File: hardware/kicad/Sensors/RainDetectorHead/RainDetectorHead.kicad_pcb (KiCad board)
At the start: 2 copper layers, 54.1 x 44.1 mm, 27 parts, among them J1 Conn_01x04_Pin, J2 Conn_01x04_Pin

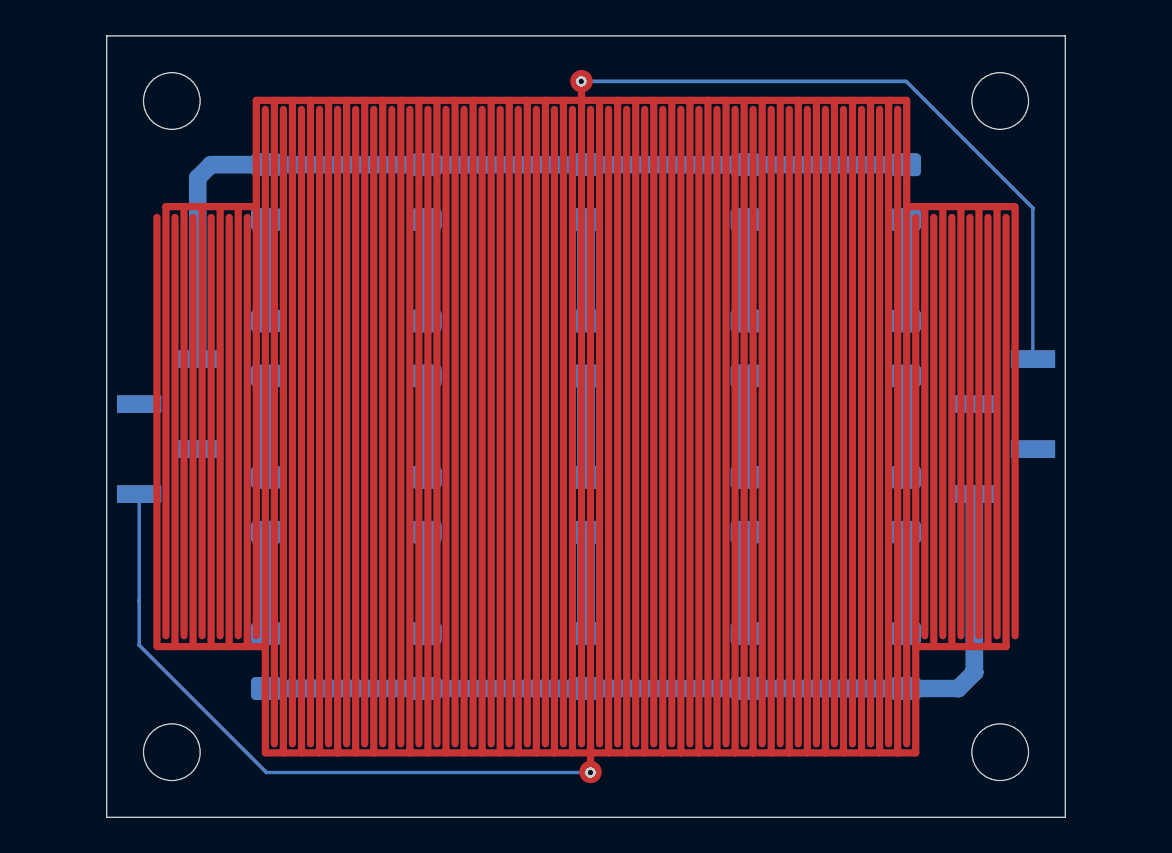
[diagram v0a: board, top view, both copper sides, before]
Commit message: modified Board-Geometry for RainDetector Head & Controller
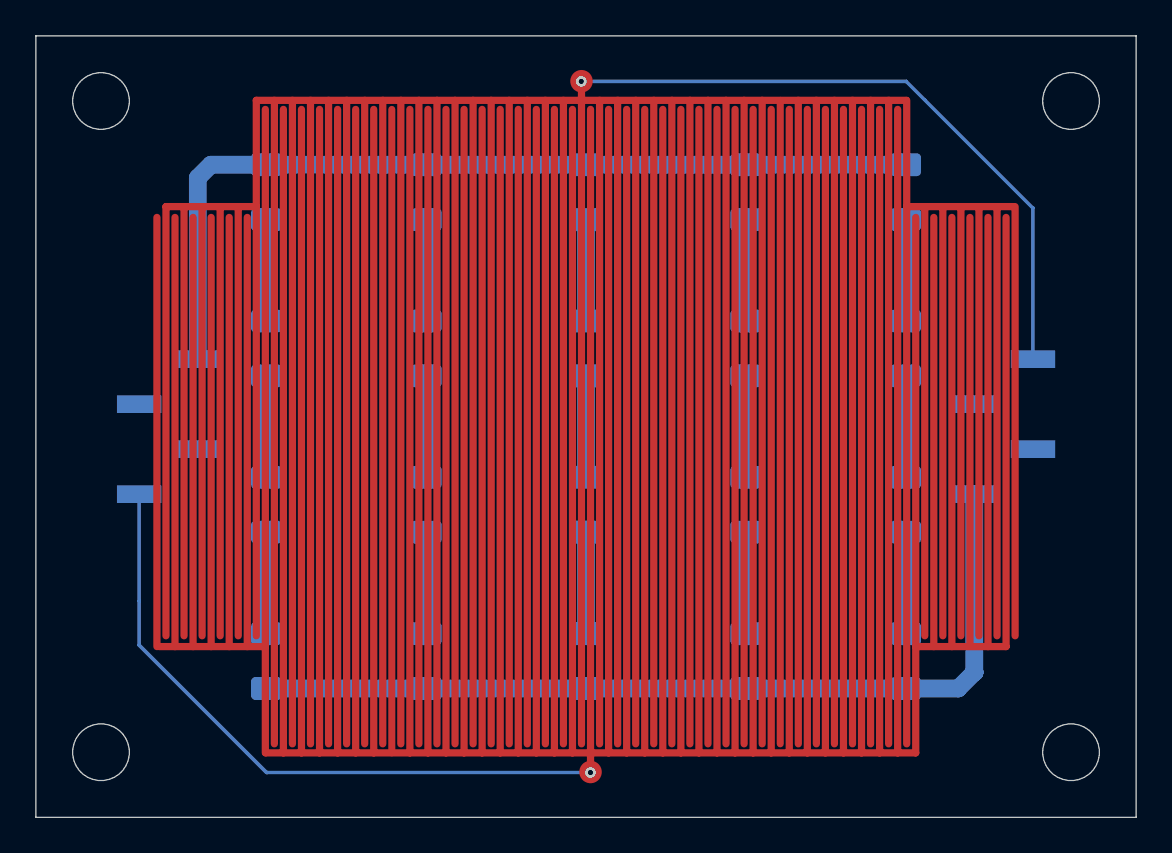
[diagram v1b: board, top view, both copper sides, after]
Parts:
- moved H1 4.00 mm to (159.7, 93.7)
- moved H2 4.00 mm to (214.4, 93.7)
- moved H3 4.00 mm to (214.4, 130.4)
- moved H4 4.00 mm to (159.7, 130.4)
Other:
- board size 54.1 x 44.1 mm -> 62.1 x 44.1 mm
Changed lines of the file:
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@@
 			(outputformat 1)
 			(mirror no)
-			(drillshape 1)
+			(drillshape 0)
 			(scaleselection 1)
-			(outputdirectory "")
+			(outputdirectory "Gerber")
 		)
 	)
@@
 	(footprint "MountingHole:MountingHole_3.2mm_M3"
 		(layer "F.Cu")
-		(at 163.676955 93.676955)
+		(at 159.676955 93.676955)
 		(descr "Mounting Hole 3.2mm, M3, no annular, generated by kicad-footprint-generator mountinghole.py")
 		(tags "mountinghole M3")
@@
 	(footprint "MountingHole:MountingHole_3.2mm_M3"
 		(layer "F.Cu")
-		(at 210.443045 93.676955)
+		(at 214.443045 93.676955)
 		(descr "Mounting Hole 3.2mm, M3, no annular, generated by kicad-footprint-generator mountinghole.py")
 		(tags "mountinghole M3")
@@
 	(footprint "MountingHole:MountingHole_3.2mm_M3"
 		(layer "F.Cu")
-		(at 210.443045 130.443045)
+		(at 214.443045 130.443045)
 		(descr "Mounting Hole 3.2mm, M3, no annular, generated by kicad-footprint-generator mountinghole.py")
 		(tags "mountinghole M3")
@@
 	(footprint "MountingHole:MountingHole_3.2mm_M3"
 		(layer "F.Cu")
-		(at 163.676955 130.443045)
+		(at 159.676955 130.443045)
 		(descr "Mounting Hole 3.2mm, M3, no annular, generated by kicad-footprint-generator mountinghole.py")
 		(tags "mountinghole M3")
@@
 	)
 	(footprint "Connector_PinHeader_2.54mm:PinHeader_1x04_P2.54mm_Vertical_SMD_Pin1Left"
-		(locked yes)
 		(layer "B.Cu")
 		(at 163.485 112.06 180)
@@
 			(type default)
 		)
+		(locked yes)
 		(layer "Dwgs.User")
 	)
@@
 	)
 	(gr_line
-		(start 160 86.595)
-		(end 160 137.525)
+		(start 156 86.595)
+		(end 156 137.525)
 		(stroke
 			(width 0.1)
@@
 	)
 	(gr_line
-		(start 160 90)
-		(end 163.676955 93.676955)
+		(start 156 90)
+		(end 159.676955 93.676955)
 		(stroke
 			(width 0.1)
@@
 	)
 	(gr_line
-		(start 160 134.12)
-		(end 163.676955 130.443045)
+		(start 156 134.12)
+		(end 159.676955 130.443045)
 		(stroke
 			(width 0.1)
@@
 			(type default)
 		)
+		(locked yes)
 		(layer "Dwgs.User")
 	)
@@
 	)
 	(gr_line
-		(start 214.12 86.595)
-		(end 214.12 137.525)
+		(start 218.12 86.595)
+		(end 218.12 137.525)
 		(stroke
 			(width 0.1)
@@
 	)
 	(gr_line
-		(start 214.12 90)
-		(end 210.443045 93.676955)
+		(start 218.12 90)
+		(end 214.443045 93.676955)
 		(stroke
 			(width 0.1)
@@
 	)
 	(gr_rect
-		(start 160 90)
-		(end 214.12 134.12)
+		(start 156 90)
+		(end 218.12 134.12)
 		(stroke
 			(width 0.05)

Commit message: Update RainDetector board connectors, outlines and parts kits
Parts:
- J1, J2: value Conn_01x04_Pin -> Conn_02x02_Odd_Even; footprint Connector_PinHeader_2.54mm:PinHeader_1x04_P2.54mm_Vertical_SMD_Pin1Left -> Connector_PinHeader_2.54mm:PinHeader_2x02_P2.54mm_Vertical_SMD
- turned J1 to -90 degrees
- turned J2 to -90 degrees
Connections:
- J2 pad 1: /HEATER- -> /SENSE
- J2 pad 4: /SENSE -> /HEATER-
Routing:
- net /HEATER+: track 50.5 -> 53.2 mm
- net /HEATER-: track 50.9 -> 53.3 mm
